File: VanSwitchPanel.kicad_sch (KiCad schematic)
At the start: 16 parts, among them J1 Screw_Terminal_01x05, J2 Screw_Terminal_01x02, J3 Screw_Terminal_01x05, J4 Conn_01x02_Socket, J5 Screw_Terminal_01x02, J6 Conn_01x02_Socket, K1 Relay_SPST-NO, K2 Relay_SPST-NO, K3 Relay_SPST-NO, K4 Relay_SPST-NO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

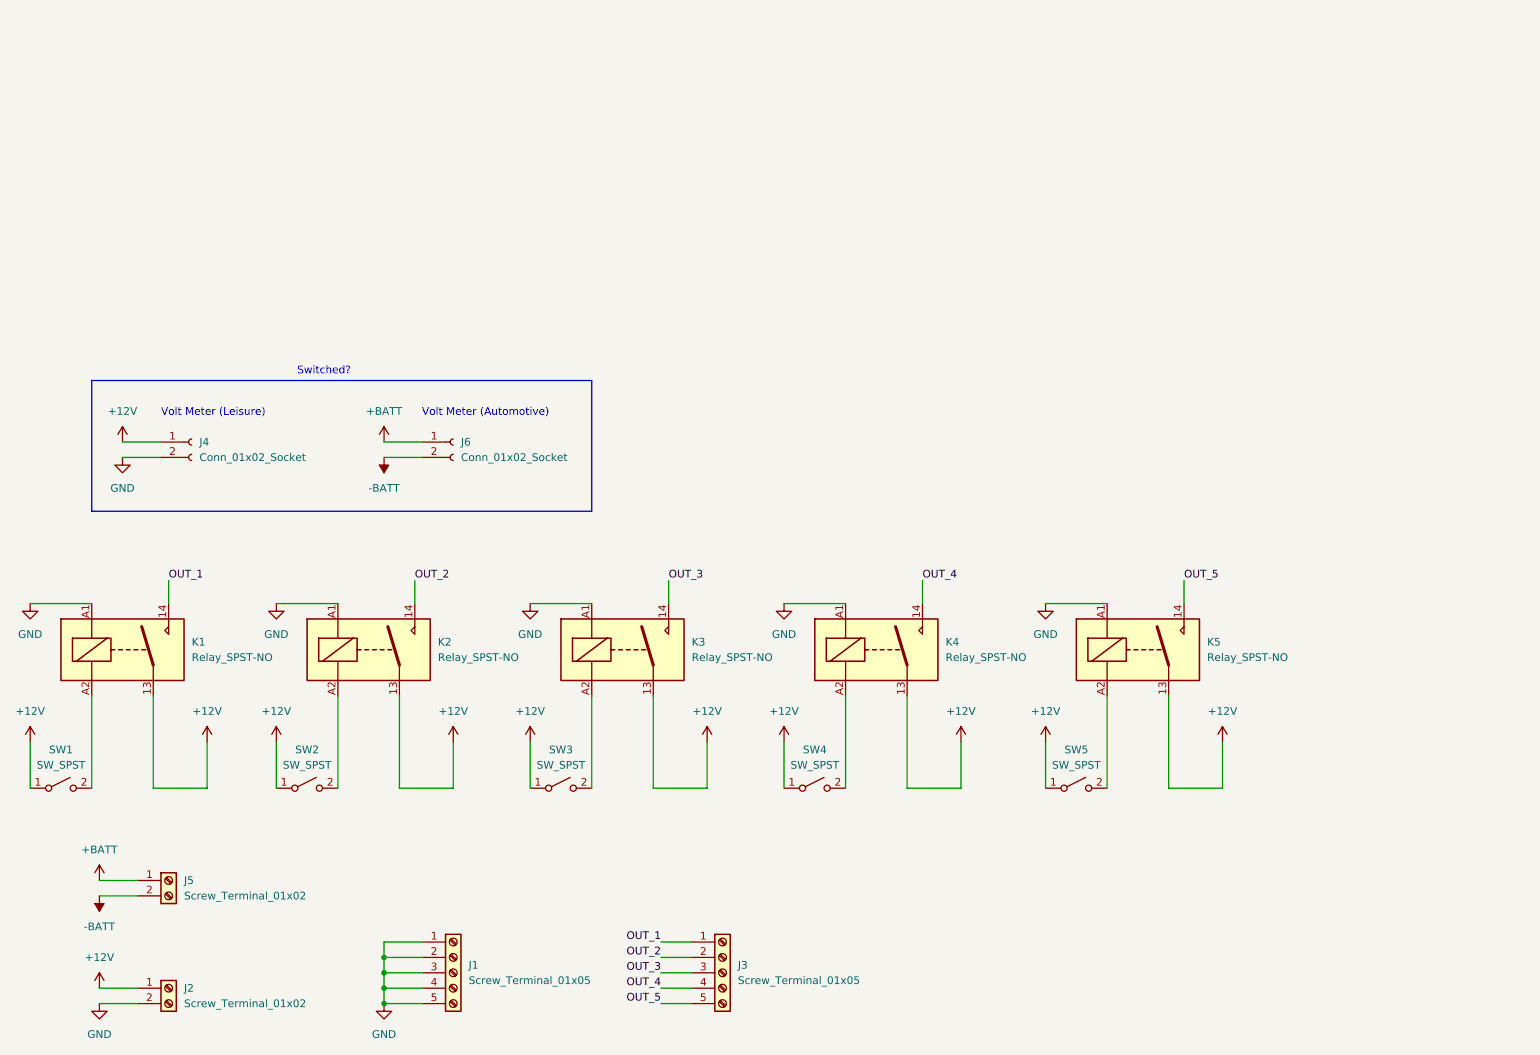
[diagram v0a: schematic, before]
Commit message: Add switched supply voltages
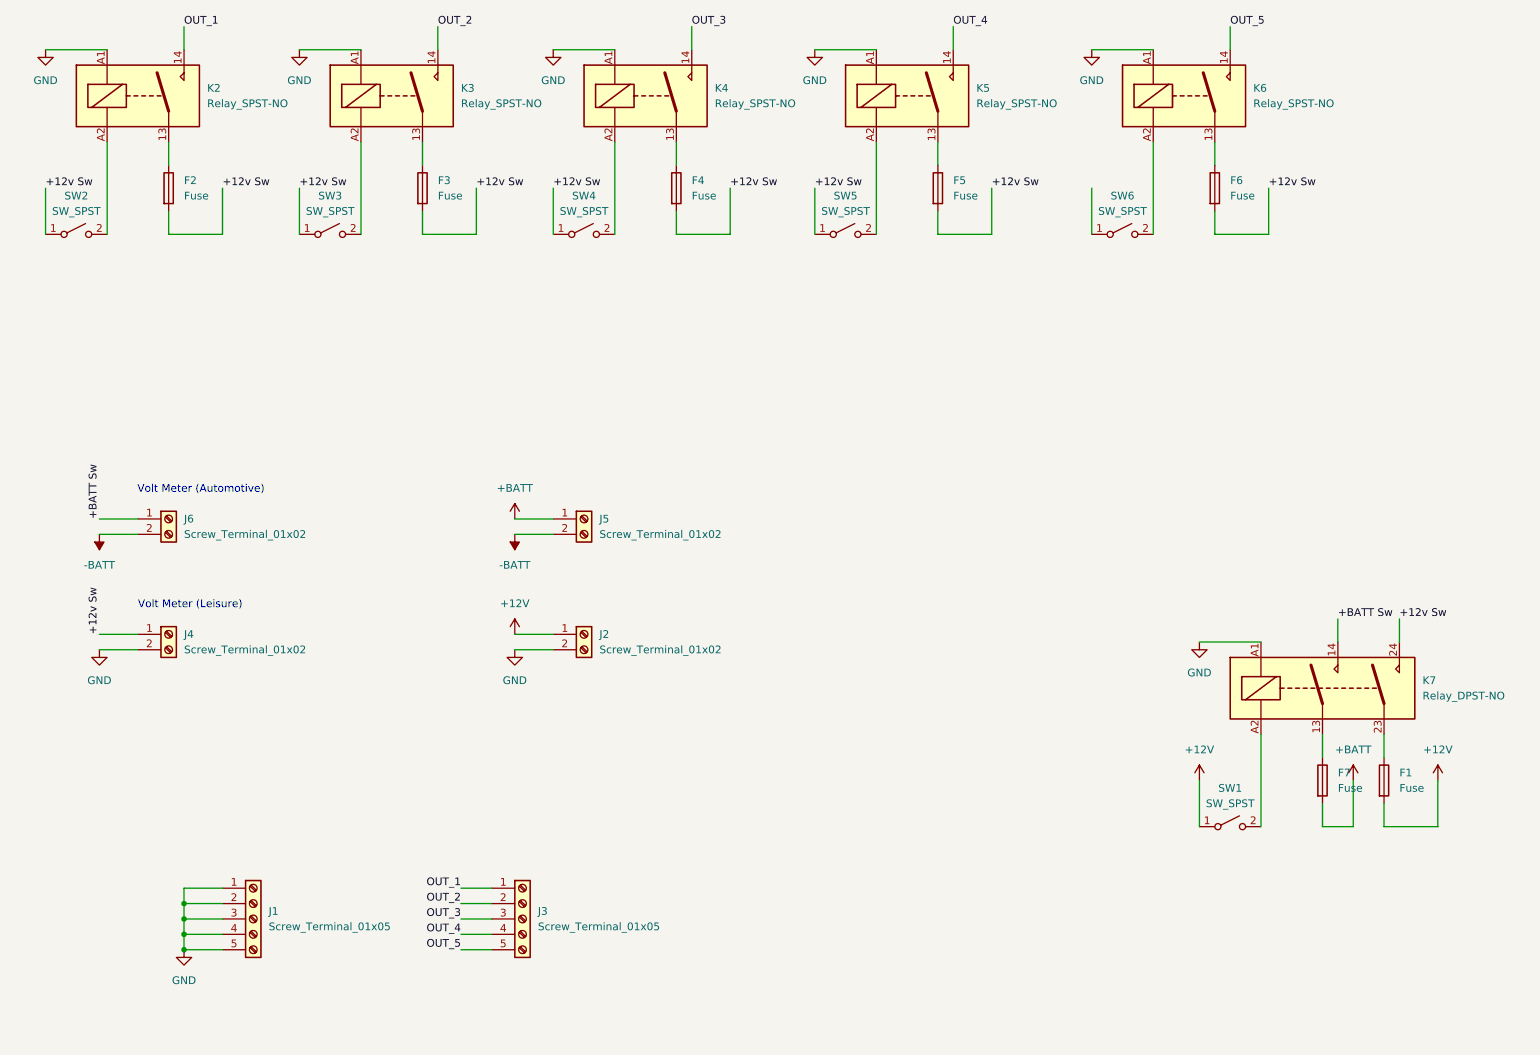
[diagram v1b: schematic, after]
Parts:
- removed J4, J6: Conn_01x02_Socket, symbol Connector:Conn_01x02_Socket
- removed K1: Relay_SPST-NO, symbol Relay:Relay_SPST-NO
- added F1, F2, F3, F4, F5, F6, F7: Fuse, symbol Device:Fuse
- added J4, J6: Screw_Terminal_01x02, symbol Connector:Screw_Terminal_01x02
- added K6: Relay_SPST-NO, Relay_THT:Relay_SPST_Omron_G2RL-1A, symbol Relay:Relay_SPST-NO
- added K7: Relay_DPST-NO, Relay_THT:Relay_DPST_Omron_G2RL-2A, symbol Relay:Relay_DPST-NO
- added SW6: SW_SPST, symbol Switch:SW_SPST
- K2, K3, K4, K5: footprint (none) -> Relay_THT:Relay_SPST_Omron_G2RL-1A
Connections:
- net +12V: now also F1.2; no longer K2.13, K3.13, K4.13, K5.13, SW2.1 (A), SW3.1 (A), SW4.1 (A), SW5.1 (A)
- net +BATT: now also F7.2
- net -BATT: now also J6.2 (Pin_2)
- net GND: now also J4.2 (Pin_2), K6.A1, K7.A1
- net OUT_1: now also K2.14
- net OUT_2: now also K3.14; no longer K2.14
- net OUT_3: now also K4.14; no longer K3.14
- net OUT_4: now also K5.14; no longer K4.14
- net OUT_5: now also K6.14; no longer K5.14
- net at SW1.2 (B): now also K7.A2
- new net: F5.1, K5.13
- new net: F6.1, K6.13
- new net: F2.1, K2.13
- new net: K6.A2, SW6.2 (B)
- new net: F7.1, K7.13
- new net: F4.1, K4.13
- new net: F3.1, K3.13
- new net: F1.1, K7.23
- new net +12v Sw: F2.2, F3.2, F4.2, F5.2, F6.2, J4.1 (Pin_1), K7.24, SW2.1 (A), SW3.1 (A), SW4.1 (A), SW5.1 (A)
- new net +BATT Sw: J6.1 (Pin_1), K7.14
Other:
- note removed: "Switched?"
- moved on the sheet: J1, J2, J3, J5, K2, K3, K4, K5, SW1, SW2, SW3, SW4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

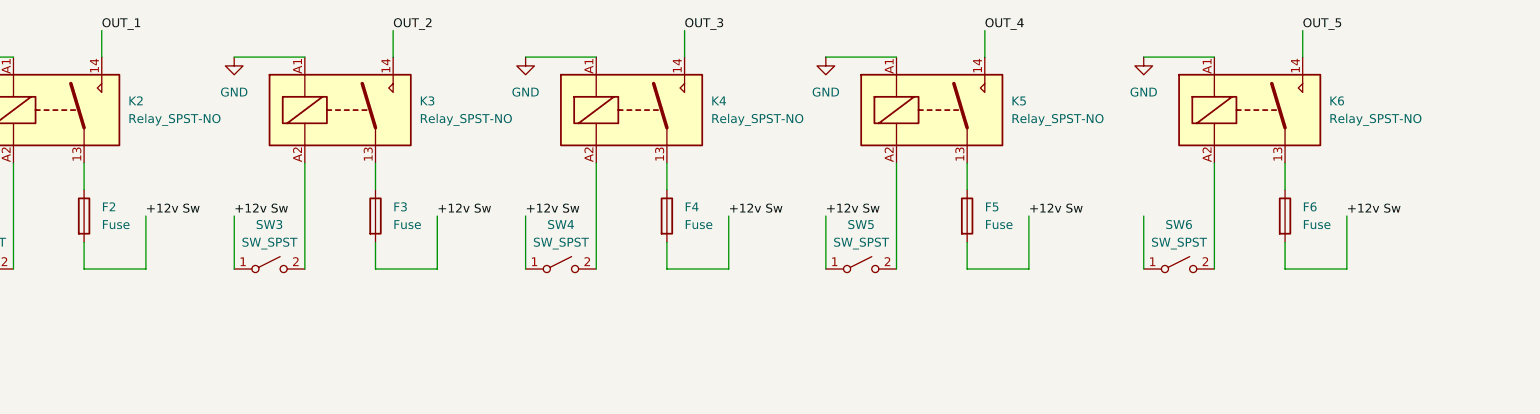
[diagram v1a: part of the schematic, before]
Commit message: Do not feed all supplies through main relay
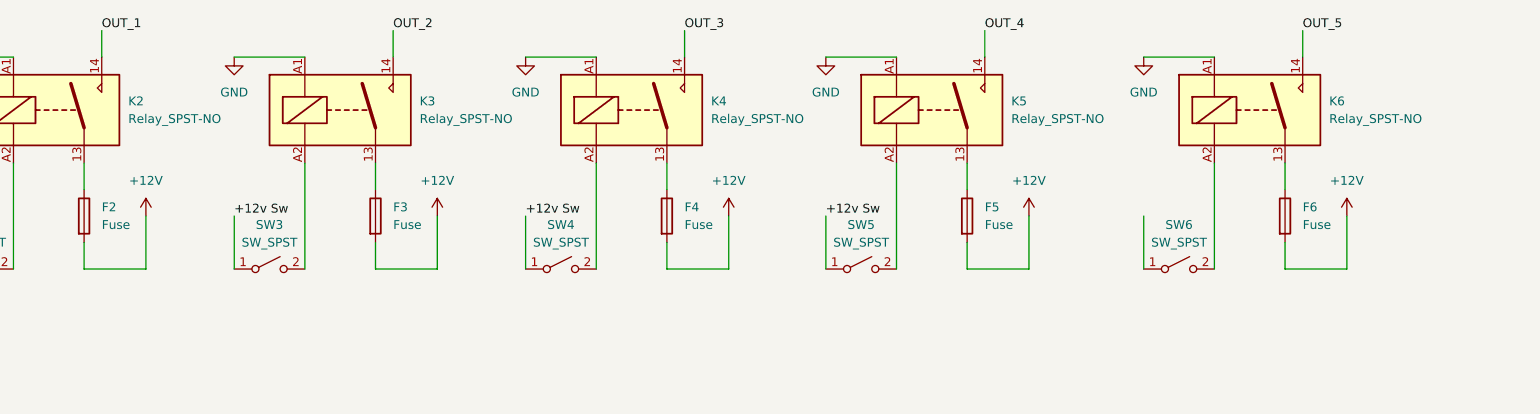
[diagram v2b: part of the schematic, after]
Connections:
- net +12V: now also F2.2, F3.2, F4.2, F5.2, F6.2
- net +12v Sw: no longer F2.2, F3.2, F4.2, F5.2, F6.2

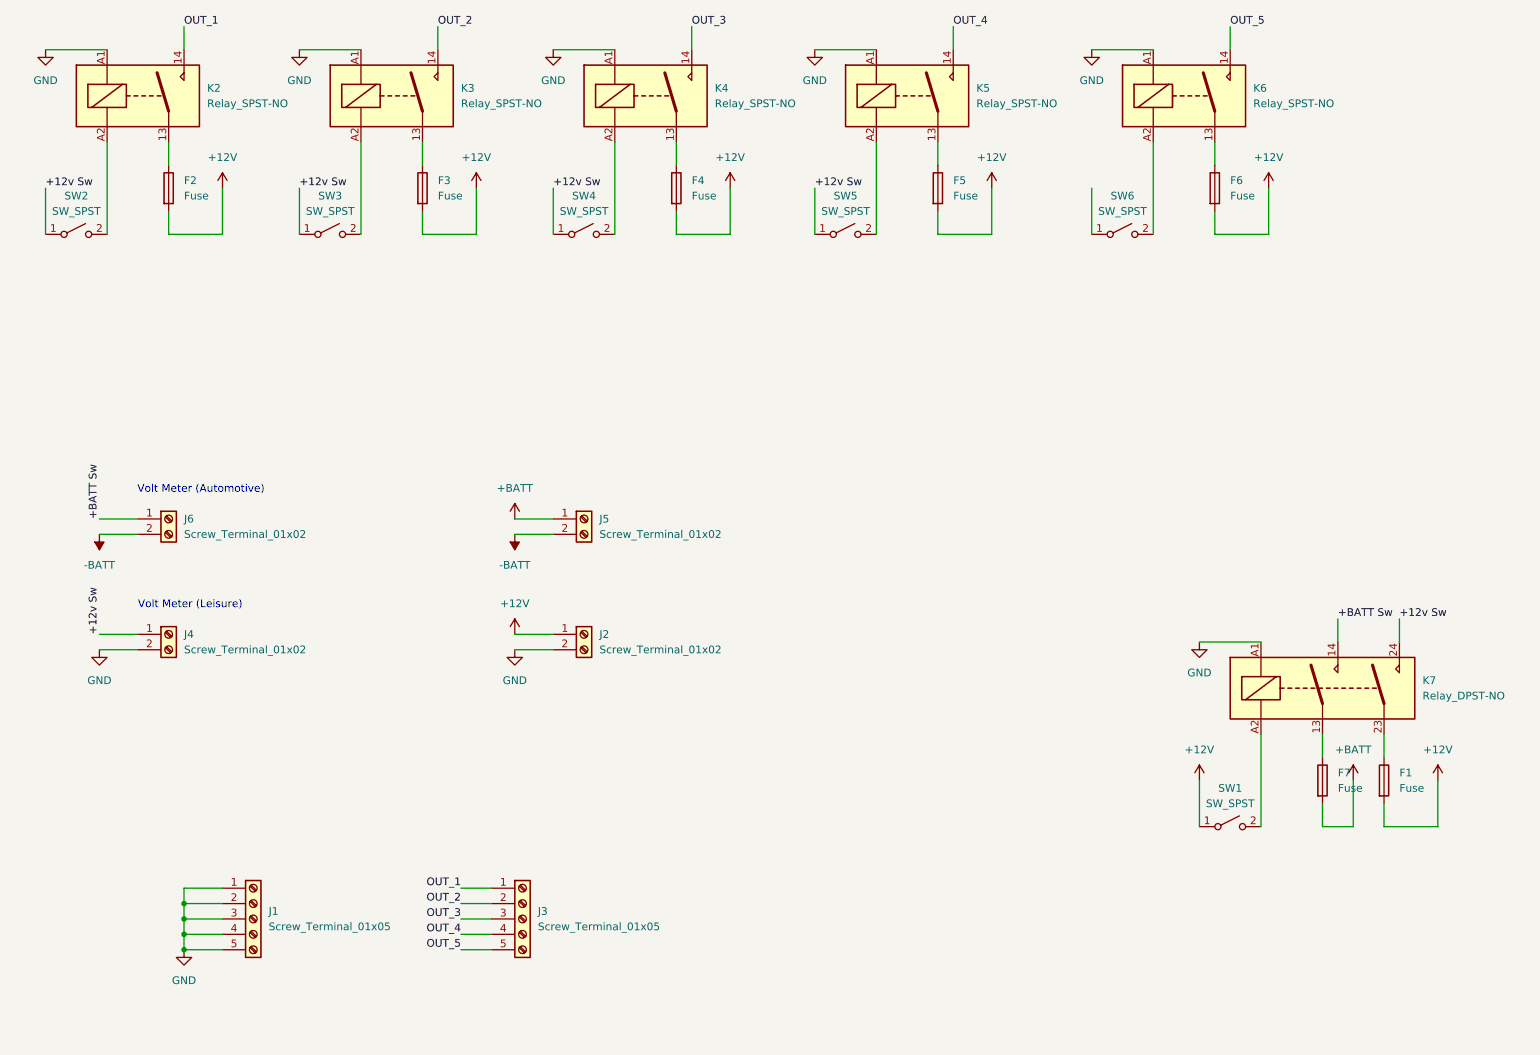
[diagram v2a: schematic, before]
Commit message: Add pcb and footprints
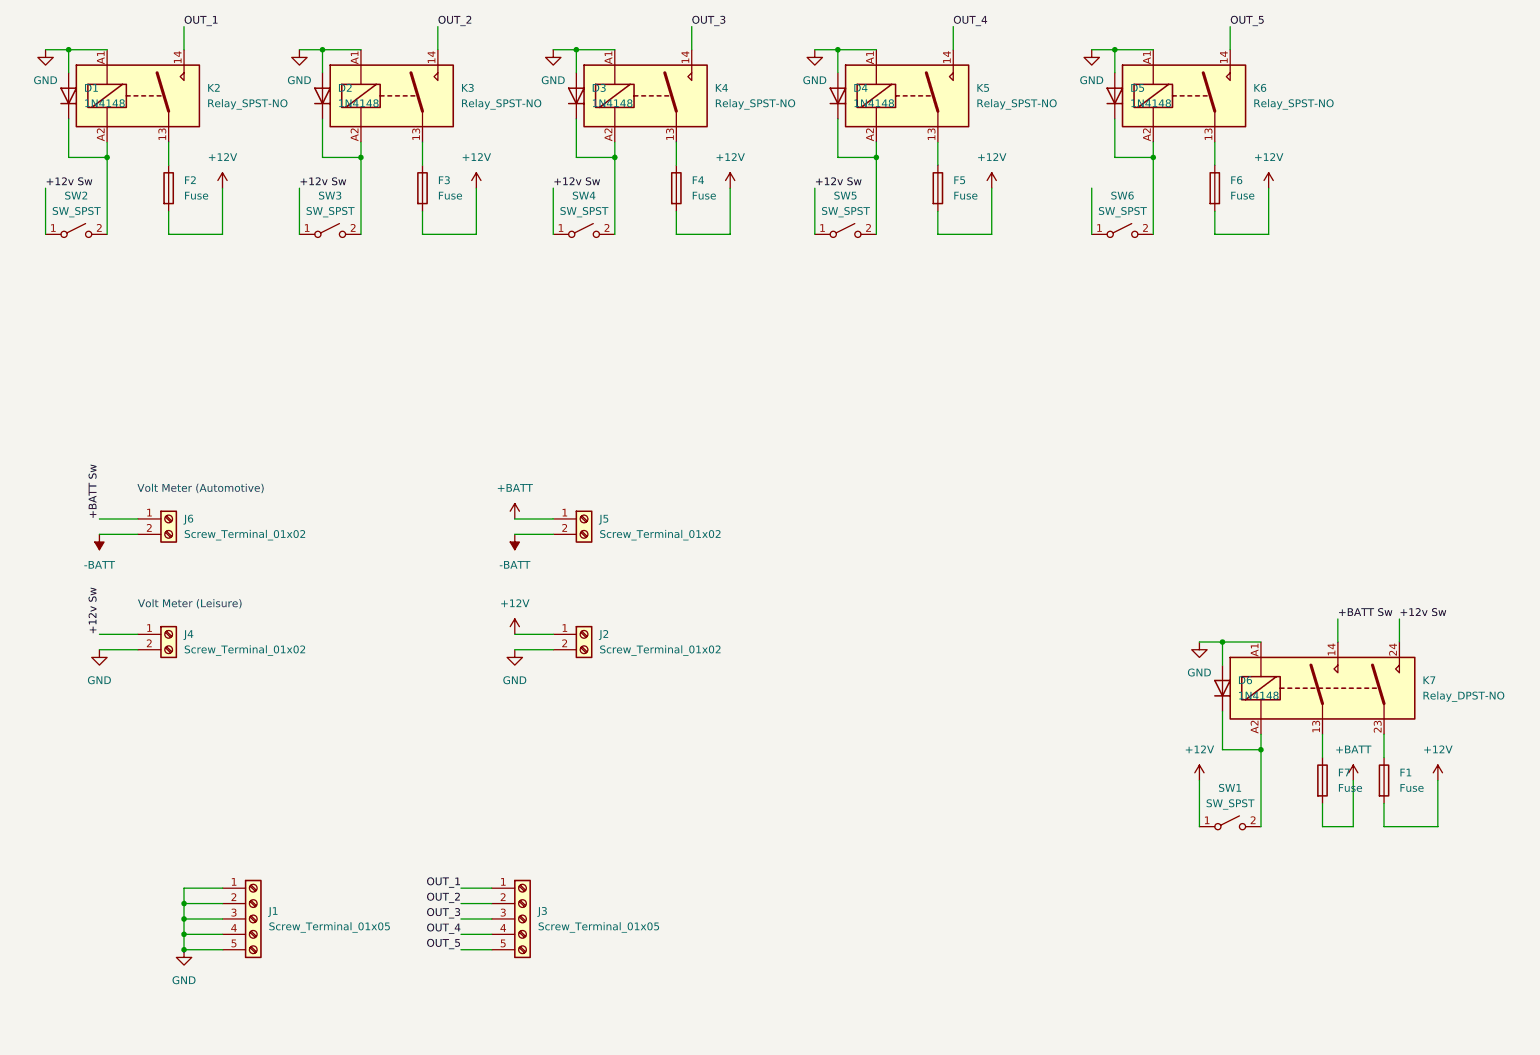
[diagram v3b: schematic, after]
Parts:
- added D1, D2, D3, D4, D5, D6: 1N4148, Diode_THT:D_DO-35_SOD27_P7.62mm_Horizontal, symbol Diode:1N4148
- J1, J3: footprint (none) -> TerminalBlock_Phoenix:TerminalBlock_Phoenix_MKDS-1,5-5-5.08_1x05_P5.08mm_Horizontal
- J2, J4, J5, J6: footprint (none) -> TerminalBlock_Phoenix:TerminalBlock_Phoenix_MKDS-1,5-2-5.08_1x02_P5.08mm_Horizontal
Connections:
- net GND: now also D1.2 (A), D2.2 (A), D3.2 (A), D4.2 (A), D5.2 (A), D6.2 (A)
- net at K3.A2, SW3.2 (B): now also D2.1 (K)
- net at K4.A2, SW4.2 (B): now also D3.1 (K)
- net at K5.A2, SW5.2 (B): now also D4.1 (K)
- net at K2.A2, SW2.2 (B): now also D1.1 (K)
- net at K7.A2, SW1.2 (B): now also D6.1 (K)
- net at K6.A2, SW6.2 (B): now also D5.1 (K)
